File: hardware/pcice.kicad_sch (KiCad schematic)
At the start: 19 parts, among them J1 CON 2X3, J2 CON 3+1, J3 PCIE X1 12V, SW1 LPTS, U1 5V SOT-89 REG, U2 ATTINY13A

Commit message: very rough sketch of i2c capable version
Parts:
- removed J1: CON 2X3, _Footprints:GENERIC_IDC_2X3, symbol Connector_Generic:Conn_02x03_Odd_Even
- removed U2: ATTINY13A, _Footprints:SOIC-8, symbol MCU_Microchip_ATtiny:ATtiny13A-SS
- added D5, D6: 5V1, symbol Device:D_Zener
- added J1: Conn_01x03, symbol Connector_Generic:Conn_01x03
- added R6: 220, _Footprints:R_0805, symbol Device:R
- added U2: ATtiny1616-M, Package_SO:SOIC-20W_7.5x12.8mm_P1.27mm, symbol MCU_Microchip_ATtiny:ATtiny1616-M
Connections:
- net +5V: now also J1.3 (Pin_3), U2.4 (VCC)
- net GND: now also D5.2 (A), D6.2 (A), J1.1 (Pin_1), U2.21 (GND), U2.3 (GND)
- net RESET: now also J1.2 (Pin_2), U2.19 (~{RESET}/PA0)
- net at J2.3 (Pin_3): now also R6.2
- net PB0 renamed LED_A
- net PB1 renamed FAN_PWM
- net FAN_PWM: now also D5.1 (K), U2.5 (PA4)
- net PB3 renamed LED_B
- new net FAN_TACH: D6.1 (K), R6.1, U2.8 (PA7)
- new net RxD: U2.11 (PB3)
- new net SCL: U2.14 (PB0)
- new net SDA: U2.13 (PB1)
- new net TxD: U2.12 (PB2)
- no-connect marks 1 -> 11
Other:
- note added: "PROTECTION"
- note added: "TODO: Add UART header"
- note added: "TODO: add NTC"
- note added: "TODO: limit I2C to 3v3"
- moved on the sheet: C3, R4

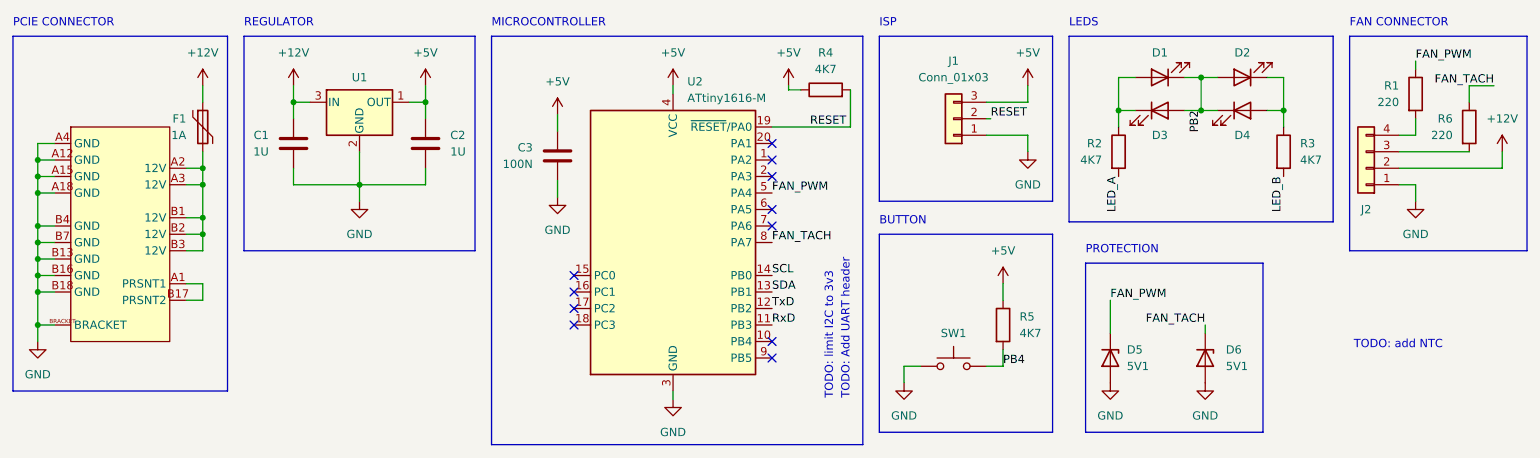
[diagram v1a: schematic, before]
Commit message: add ntc
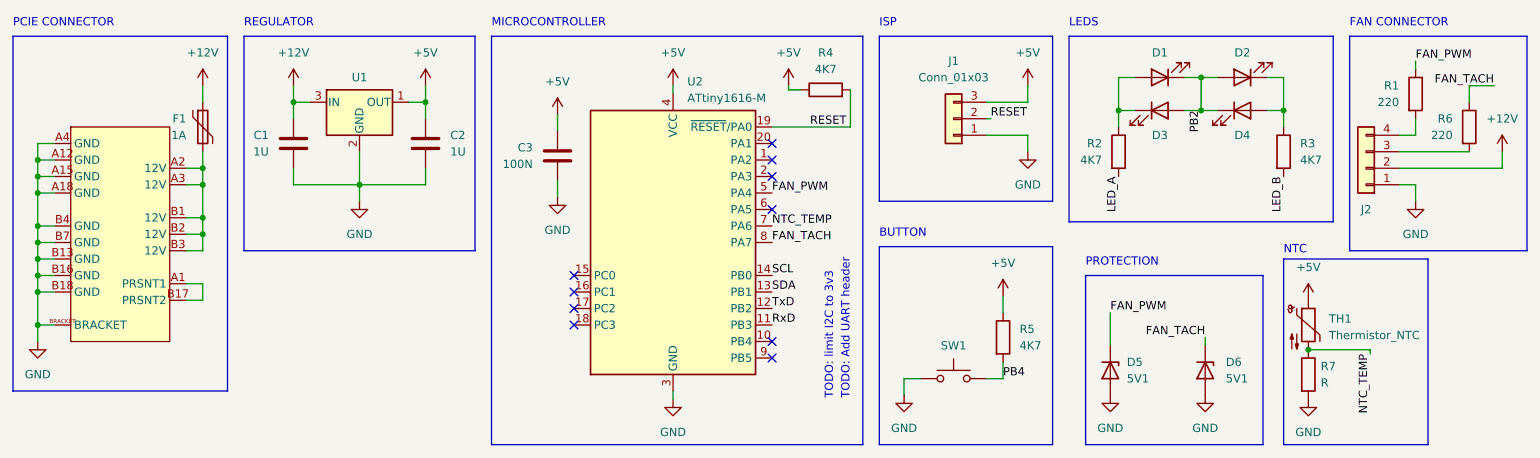
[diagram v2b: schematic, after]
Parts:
- added R7: R, symbol Device:R
- added TH1: Thermistor_NTC, symbol Device:Thermistor_NTC
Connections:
- net +5V: now also TH1.1
- net GND: now also R7.2
- net NTC_TEMP: now reaches U2.7 (PA6)
- net NTC_TEMP: now also R7.1, TH1.2
- no-connect marks 11 -> 10
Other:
- note added: "NTC"
- note removed: "TODO: add NTC"
- moved on the sheet: D5, D6, R5, SW1
